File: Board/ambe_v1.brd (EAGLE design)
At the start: 48.9 x 52.1 mm, 33 parts, among them IC3 AMBE-3000LQFP-128

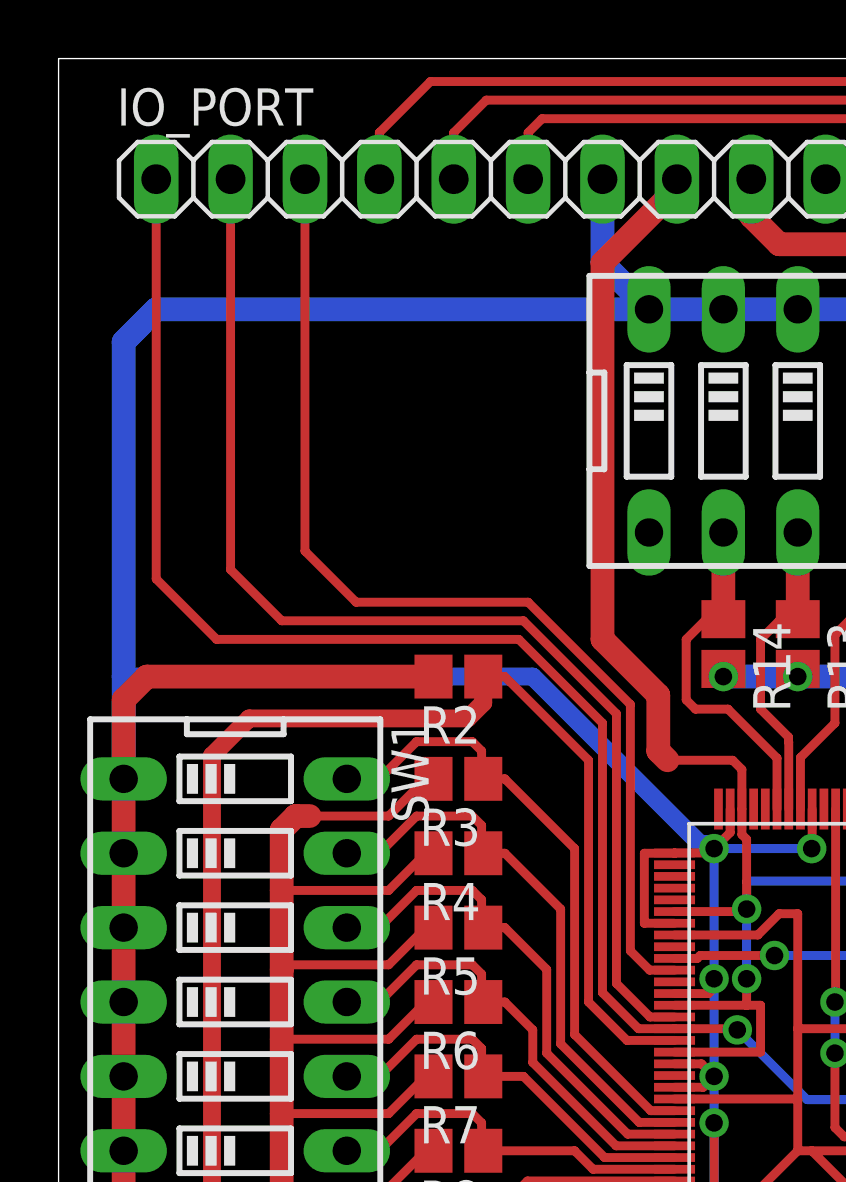
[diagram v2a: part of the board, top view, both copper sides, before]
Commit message: + pull up to AMBE's Reset & progress in ModemIO brd
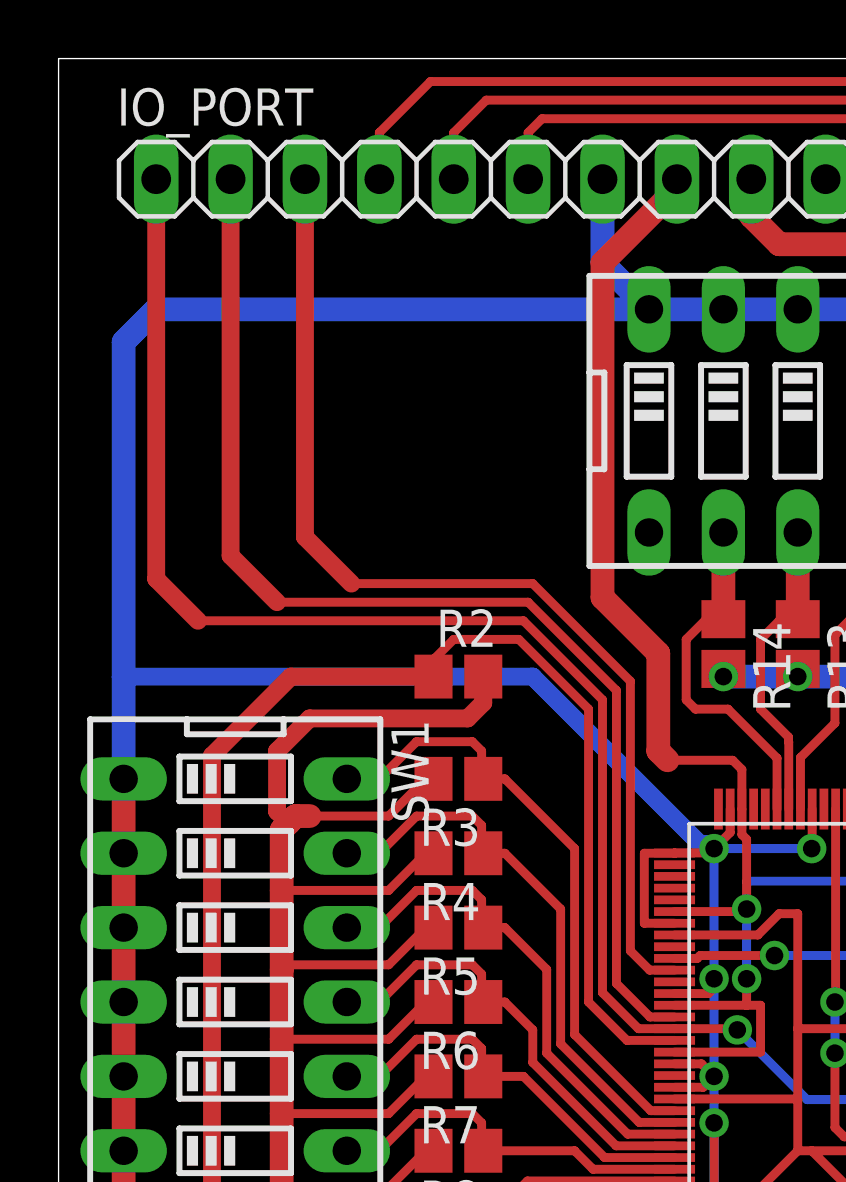
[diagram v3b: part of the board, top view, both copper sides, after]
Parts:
- turned R2 to 0 degrees
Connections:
- net 3V3: now also R2.2
- net GND: no longer R2.2
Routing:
- net GND: track 231.6 -> 218.0 mm
- net 3V3: track 191.8 -> 203.0 mm
- net DSP_RESET: track 54.2 -> 56.1 mm
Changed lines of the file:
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@@
 <element name="C10" library="resistor" package="C0805" value="C0.1uF 10V" x="40.3225" y="11.1125"/>
 <element name="C11" library="resistor" package="C0805" value="C0.1uF 10V" x="40.3225" y="8.89"/>
-<element name="R2" library="resistor" package="R0805" value="R10K" x="13.6525" y="30.95625" rot="R180"/>
+<element name="R2" library="resistor" package="R0805" value="R10K" x="13.6525" y="30.95625"/>
 <element name="SW1" library="SparkFun-Electromechanical" package="DIPSWITCH-08" value="" x="6.0325" y="18.57375" rot="R270"/>
 <element name="R3" library="resistor" package="R0805" value="R10K" x="13.6525" y="27.46375" rot="R180"/>
@@
 <wire x1="11.27125" y1="10.95375" x2="7.62" y2="10.95375" width="0.3048" layer="1"/>
 <wire x1="7.62" y1="23.65375" x2="7.62" y2="25.7175" width="0.8128" layer="1"/>
-<wire x1="7.62" y1="25.7175" x2="8.09625" y2="26.19375" width="0.8128" layer="1"/>
+<wire x1="7.62" y1="25.7175" x2="7.858125" y2="25.955625" width="0.8128" layer="1"/>
+<wire x1="7.858125" y1="25.955625" x2="8.09625" y2="26.19375" width="0.8128" layer="1"/>
 <wire x1="8.09625" y1="26.19375" x2="8.5725" y2="26.19375" width="0.8128" layer="1"/>
 <wire x1="11.27125" y1="26.19375" x2="8.5725" y2="26.19375" width="0.3048" layer="1"/>
@@
 <wire x1="25.24125" y1="30.95625" x2="25.24125" y2="31.2175" width="0.6096" layer="1"/>
 <wire x1="27.78125" y1="30.95625" x2="27.78125" y2="31.2175" width="0.6096" layer="1"/>
+<contactref element="R2" pad="2"/>
+<wire x1="14.5025" y1="30.95625" x2="14.5025" y2="30.06" width="0.6096" layer="1"/>
+<wire x1="14.5025" y1="30.06" x2="13.97" y2="29.5275" width="0.6096" layer="1"/>
+<wire x1="13.97" y1="29.5275" x2="8.5725" y2="29.5275" width="0.6096" layer="1"/>
+<wire x1="8.5725" y1="29.5275" x2="7.46125" y2="28.41625" width="0.6096" layer="1"/>
+<wire x1="7.46125" y1="28.41625" x2="7.46125" y2="26.3525" width="0.6096" layer="1"/>
+<wire x1="7.46125" y1="26.3525" x2="7.858125" y2="25.955625" width="0.6096" layer="1"/>
 </signal>
 <signal name="VREF_1V">
@@
 <contactref element="C10" pad="2"/>
 <contactref element="C11" pad="2"/>
-<contactref element="R2" pad="2"/>
 <contactref element="SW1" pad="8"/>
 <contactref element="SW1" pad="7"/>
@@
 <wire x1="26.82875" y1="12.3825" x2="22.38375" y2="12.3825" width="0.3048" layer="16"/>
 <wire x1="22.38375" y1="12.3825" x2="22.38375" y2="15.71625" width="0.3048" layer="16"/>
-<wire x1="12.8025" y1="30.95625" x2="3.01625" y2="30.95625" width="0.8128" layer="1"/>
-<wire x1="3.01625" y1="30.95625" x2="2.2225" y2="30.1625" width="0.8128" layer="1"/>
-<wire x1="2.2225" y1="30.1625" x2="2.2225" y2="27.46375" width="0.8128" layer="1"/>
 <wire x1="18.0975" y1="10.375" x2="20.32" y2="10.375" width="0.8128" layer="1"/>
 <wire x1="21.03375" y1="12.5325" x2="21.03375" y2="11.08875" width="0.3048" layer="1"/>
@@
 <wire x1="18.57375" y1="47.9425" x2="18.57375" y2="45.085" width="0.8128" layer="16"/>
 <wire x1="18.57375" y1="45.085" x2="20.16125" y2="43.4975" width="0.8128" layer="16"/>
-<wire x1="2.2225" y1="27.46375" x2="2.2225" y2="30.95625" width="0.8128" layer="16"/>
 <wire x1="2.2225" y1="30.95625" x2="2.2225" y2="42.38625" width="0.8128" layer="16"/>
 <wire x1="2.2225" y1="42.38625" x2="3.33375" y2="43.4975" width="0.8128" layer="16"/>
@@
 <wire x1="22.225" y1="25.24125" x2="22.38375" y2="25.0825" width="0.6096" layer="16"/>
 <wire x1="25.73375" y1="25.0825" x2="25.7175" y2="25.0825" width="0.6096" layer="16"/>
+<wire x1="2.2225" y1="30.95625" x2="2.2225" y2="27.46375" width="0.8128" layer="16"/>
 </signal>
 <signal name="ADCRESEXT">
@@
 <wire x1="21.03375" y1="18.9325" x2="19.8025" y2="18.9325" width="0.3048" layer="1"/>
 <wire x1="19.8025" y1="18.9325" x2="18.57375" y2="20.16125" width="0.3048" layer="1"/>
-<wire x1="18.57375" y1="20.16125" x2="18.57375" y2="29.36875" width="0.3048" layer="1"/>
+<wire x1="18.57375" y1="20.16125" x2="18.57375" y2="30.1625" width="0.3048" layer="1"/>
 <contactref element="IO_PORT" pad="1"/>
-<wire x1="18.57375" y1="29.36875" x2="15.71625" y2="32.22625" width="0.3048" layer="1"/>
-<wire x1="15.71625" y1="32.22625" x2="5.3975" y2="32.22625" width="0.3048" layer="1"/>
-<wire x1="5.3975" y1="32.22625" x2="3.33375" y2="34.29" width="0.3048" layer="1"/>
-<wire x1="3.33375" y1="47.9425" x2="3.33375" y2="34.29" width="0.3048" layer="1"/>
+<wire x1="18.57375" y1="30.1625" x2="15.875" y2="32.86125" width="0.3048" layer="1"/>
+<wire x1="15.875" y1="32.86125" x2="4.7625" y2="32.86125" width="0.3048" layer="1"/>
+<wire x1="3.33375" y1="47.9425" x2="3.33375" y2="34.29" width="0.6096" layer="1"/>
+<wire x1="3.33375" y1="34.29" x2="4.7625" y2="32.86125" width="0.6096" layer="1"/>
 </signal>
 <signal name="STAT7">
@@
 <wire x1="21.11375" y1="47.9425" x2="21.11375" y2="47.625" width="0.8128" layer="1"/>
 <wire x1="21.11375" y1="47.625" x2="18.57375" y2="45.085" width="0.8128" layer="1"/>
-<wire x1="18.57375" y1="45.085" x2="18.57375" y2="32.22625" width="0.8128" layer="1"/>
-<wire x1="18.57375" y1="32.22625" x2="20.47875" y2="30.32125" width="0.8128" layer="1"/>
-<wire x1="20.47875" y1="30.32125" x2="20.47875" y2="28.41625" width="0.8128" layer="1"/>
+<wire x1="20.47875" y1="31.75" x2="20.47875" y2="28.41625" width="0.8128" layer="1"/>
 <wire x1="20.47875" y1="28.41625" x2="20.79625" y2="28.09875" width="0.8128" layer="1"/>
 <wire x1="23.33375" y1="26.4325" x2="23.33375" y2="27.78375" width="0.3048" layer="1"/>
 <wire x1="23.33375" y1="27.78375" x2="23.01875" y2="28.09875" width="0.3048" layer="1"/>
 <wire x1="23.01875" y1="28.09875" x2="20.79625" y2="28.09875" width="0.3048" layer="1"/>
+<wire x1="18.57375" y1="45.085" x2="18.57375" y2="33.655" width="0.8128" layer="1"/>
+<wire x1="18.57375" y1="33.655" x2="20.47875" y2="31.75" width="0.8128" layer="1"/>
 </signal>
 <signal name="STAT/CONFIG0">
@@
 <wire x1="21.03375" y1="20.9325" x2="20.18375" y2="20.9325" width="0.3048" layer="1"/>
 <wire x1="20.18375" y1="20.9325" x2="19.52625" y2="21.59" width="0.3048" layer="1"/>
-<wire x1="19.52625" y1="21.59" x2="19.52625" y2="30.00375" width="0.3048" layer="1"/>
+<wire x1="19.52625" y1="21.59" x2="19.52625" y2="30.7975" width="0.3048" layer="1"/>
 <contactref element="IO_PORT" pad="3"/>
-<wire x1="19.52625" y1="30.00375" x2="16.03375" y2="33.49625" width="0.3048" layer="1"/>
-<wire x1="16.03375" y1="33.49625" x2="10.16" y2="33.49625" width="0.3048" layer="1"/>
-<wire x1="8.41375" y1="47.9425" x2="8.41375" y2="35.2425" width="0.3048" layer="1"/>
-<wire x1="8.41375" y1="35.2425" x2="10.16" y2="33.49625" width="0.3048" layer="1"/>
+<wire x1="19.52625" y1="30.7975" x2="16.1925" y2="34.13125" width="0.3048" layer="1"/>
+<wire x1="16.1925" y1="34.13125" x2="10.00125" y2="34.13125" width="0.3048" layer="1"/>
+<wire x1="8.41375" y1="47.9425" x2="8.41375" y2="35.71875" width="0.6096" layer="1"/>
+<wire x1="8.41375" y1="35.71875" x2="10.00125" y2="34.13125" width="0.6096" layer="1"/>
 </signal>
 <signal name="UART0_CHAN_TX">
@@
 <wire x1="21.03375" y1="19.3325" x2="20.19625" y2="19.3325" width="0.3048" layer="1"/>
 <wire x1="20.19625" y1="19.3325" x2="19.05" y2="20.47875" width="0.3048" layer="1"/>
-<wire x1="19.05" y1="20.47875" x2="19.05" y2="29.68625" width="0.3048" layer="1"/>
+<wire x1="19.05" y1="20.47875" x2="19.05" y2="30.48" width="0.3048" layer="1"/>
 <contactref element="IO_PORT" pad="2"/>
-<wire x1="19.05" y1="29.68625" x2="15.875" y2="32.86125" width="0.3048" layer="1"/>
-<wire x1="15.875" y1="32.86125" x2="7.62" y2="32.86125" width="0.3048" layer="1"/>
-<wire x1="5.87375" y1="47.9425" x2="5.87375" y2="34.6075" width="0.3048" layer="1"/>
-<wire x1="5.87375" y1="34.6075" x2="7.62" y2="32.86125" width="0.3048" layer="1"/>
+<wire x1="19.05" y1="30.48" x2="16.03375" y2="33.49625" width="0.3048" layer="1"/>
+<wire x1="5.87375" y1="47.9425" x2="5.87375" y2="35.08375" width="0.6096" layer="1"/>
+<wire x1="5.87375" y1="35.08375" x2="7.46125" y2="33.49625" width="0.6096" layer="1"/>
+<wire x1="16.03375" y1="33.49625" x2="7.46125" y2="33.49625" width="0.3048" layer="1"/>
 </signal>
 <signal name="DSP_RESET">
@@
 <wire x1="21.03375" y1="18.5325" x2="19.40875" y2="18.5325" width="0.3048" layer="1"/>
 <wire x1="19.40875" y1="18.5325" x2="18.0975" y2="19.84375" width="0.3048" layer="1"/>
-<wire x1="18.0975" y1="19.84375" x2="18.0975" y2="28.09875" width="0.3048" layer="1"/>
-<wire x1="18.0975" y1="28.09875" x2="15.24" y2="30.95625" width="0.3048" layer="1"/>
-<wire x1="15.24" y1="30.95625" x2="14.5025" y2="30.95625" width="0.3048" layer="1"/>
+<wire x1="18.0975" y1="19.84375" x2="18.0975" y2="29.845" width="0.3048" layer="1"/>
 <wire x1="3.33375" y1="2.2225" x2="3.33375" y2="5.715" width="0.6096" layer="1"/>
 <wire x1="3.33375" y1="5.715" x2="5.23875" y2="7.62" width="0.6096" layer="1"/>
 <wire x1="5.23875" y1="7.62" x2="5.23875" y2="28.2575" width="0.6096" layer="1"/>
-<wire x1="5.23875" y1="28.2575" x2="6.50875" y2="29.5275" width="0.6096" layer="1"/>
-<wire x1="14.5025" y1="30.95625" x2="14.5025" y2="30.06" width="0.6096" layer="1"/>
-<wire x1="14.5025" y1="30.06" x2="13.97" y2="29.5275" width="0.6096" layer="1"/>
-<wire x1="13.97" y1="29.5275" x2="6.50875" y2="29.5275" width="0.6096" layer="1"/>
+<wire x1="18.0975" y1="29.845" x2="15.71625" y2="32.22625" width="0.3048" layer="1"/>
+<wire x1="15.71625" y1="32.22625" x2="13.49375" y2="32.22625" width="0.3048" layer="1"/>
+<wire x1="13.49375" y1="32.22625" x2="12.85875" y2="31.59125" width="0.3048" layer="1"/>
+<wire x1="12.85875" y1="31.59125" x2="12.85875" y2="31.0125" width="0.3048" layer="1"/>
+<wire x1="12.85875" y1="31.0125" x2="12.8025" y2="30.95625" width="0.3048" layer="1"/>
+<wire x1="5.23875" y1="28.2575" x2="7.9375" y2="30.95625" width="0.6096" layer="1"/>
+<wire x1="7.9375" y1="30.95625" x2="12.8025" y2="30.95625" width="0.6096" layer="1"/>
 </signal>
 <signal name="CONFIG0">
